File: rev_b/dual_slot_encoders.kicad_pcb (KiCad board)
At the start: 2 copper layers, 50 x 25 mm, 15 parts, among them U1 GP1S094HCZ0F, U2 GP1S094HCZ0F, U3 GPS1S97HCZ0F, U4 GPS1S97HCZ0F

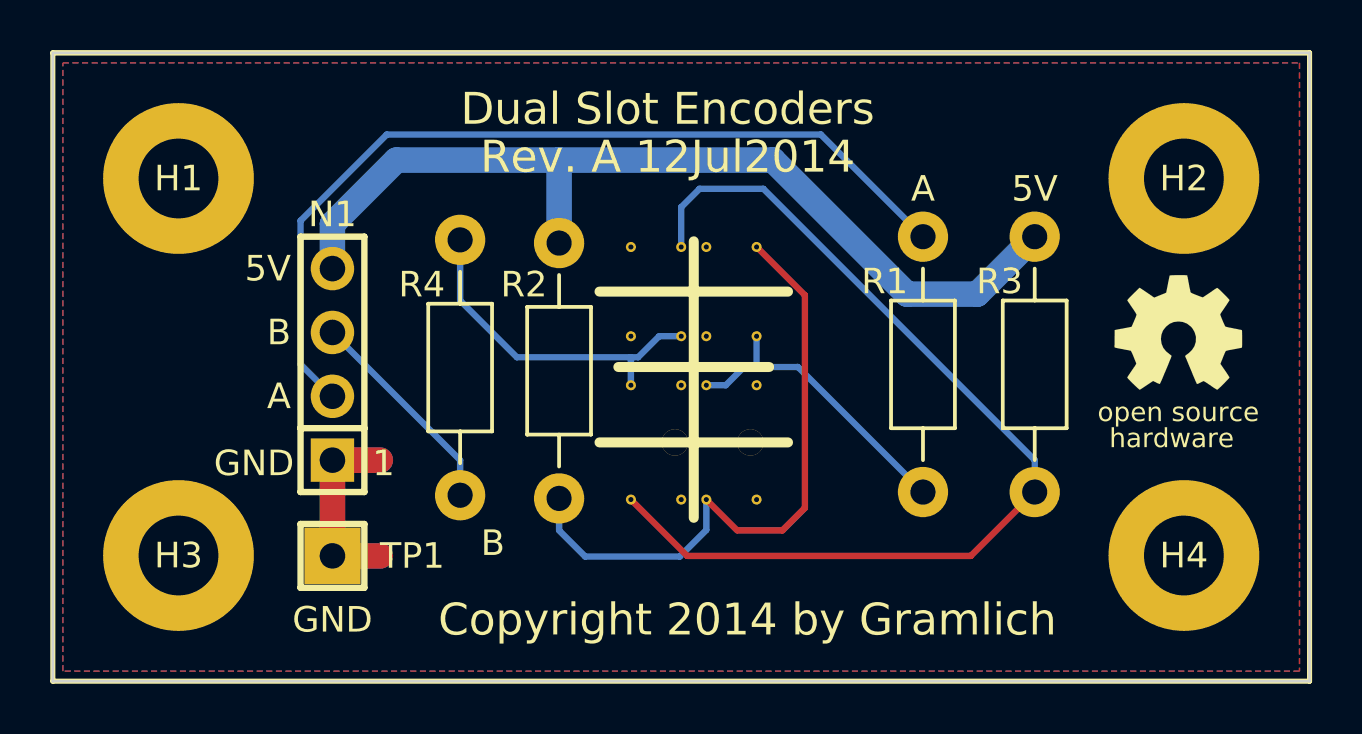
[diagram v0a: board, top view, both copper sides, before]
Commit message: Fixed interrupter lead holes.
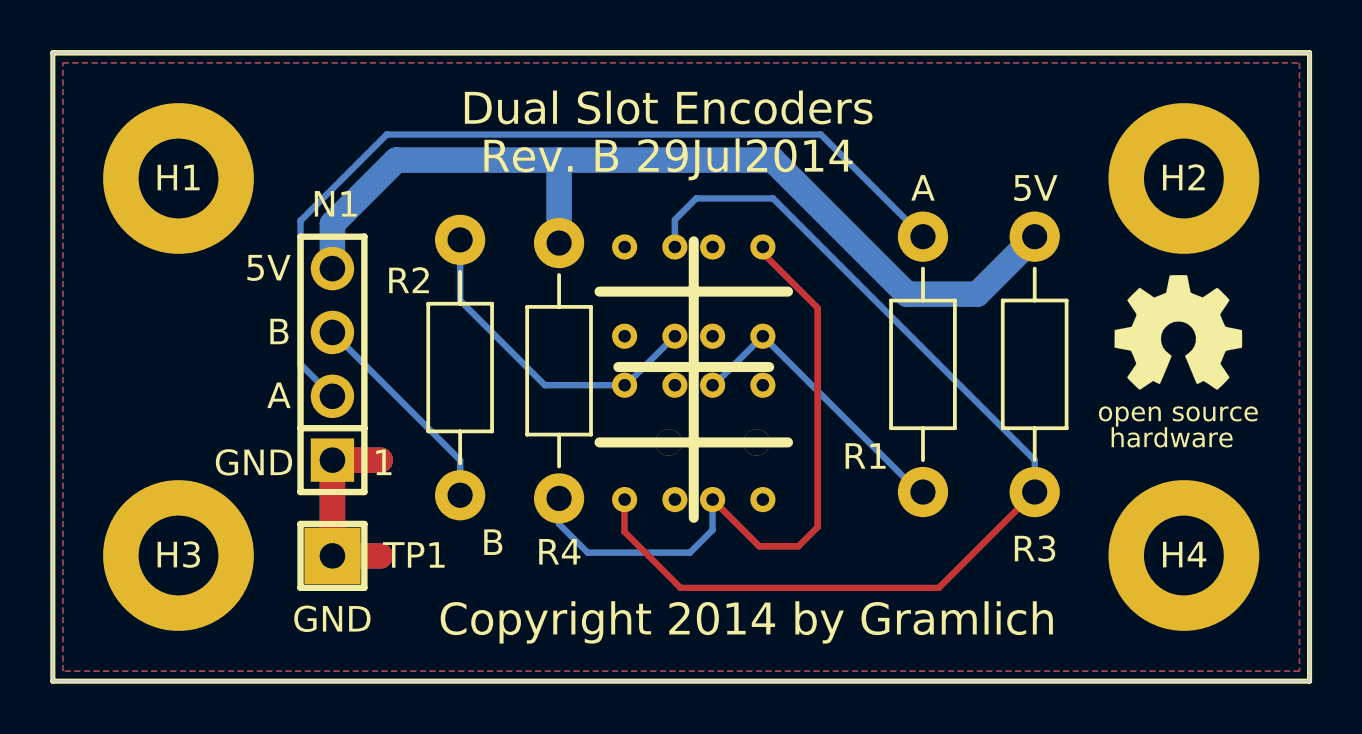
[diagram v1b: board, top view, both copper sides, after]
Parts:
- H1, H2, H3, H4: footprint Dual_Slot_Encoders_Rev_A:MountingHole_3mm -> Dual_Slot_Encoders_Rev_B:MountingHole_3mm
- N1: footprint Dual_Slot_Encoders_Rev_A:Pin_Header_Straight_1x04 -> Dual_Slot_Encoders_Rev_B:Pin_Header_Straight_1x04
- R1, R2, R3, R4: footprint Dual_Slot_Encoders_Rev_A:Resistor_Horizontal_400 -> Dual_Slot_Encoders_Rev_B:Resistor_Horizontal_400
- TP1: footprint Dual_Slot_Encoders_Rev_A:Pin_Header_Straight_1x01 -> Dual_Slot_Encoders_Rev_B:Pin_Header_Straight_1x01
- U1, U2: footprint Dual_Slot_Encoders_Rev_A:GP1S094HCZ0F -> Dual_Slot_Encoders_Rev_B:GP1S094HCZ0F
- U3, U4: footprint Dual_Slot_Encoders_Rev_A:GP1S097HCZ0F -> Dual_Slot_Encoders_Rev_B:GP1S097HCZ0F
- Z1: footprint Dual_Slot_Encoders_Rev_A:OSHW_LOGO_200mil -> Dual_Slot_Encoders_Rev_B:OSHW_LOGO_200mil
- moved U1 0.25 mm to (123.8, 115.5)
- moved U2 0.25 mm to (127.2, 115.5)
- moved U3 0.25 mm to (123.8, 109.5)
- moved U4 0.25 mm to (127.2, 109.5)
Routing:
- net Net-(R3-Pad1): track 39.7 -> 41.4 mm
- net Net-(R4-Pad1): track 25.2 -> 26.6 mm
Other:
- board text added: "Rev. B 29Jul2014"
- board text removed: "Rev. A 12Jul2014"
